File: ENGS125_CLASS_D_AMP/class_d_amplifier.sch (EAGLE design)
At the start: 23 parts, among them J1 BANANA_JACK_CT3151, J2 BANANA_JACK_CT3151, J3 BANANA_JACK_CT3151, J4 BANANA_JACK_CT3151, J5 BANANA_JACK_CT3151, J6 BANANA_JACK_CT3151, U1 LTC6992TSOT-23, U2 LTC4449

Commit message: Initial placement of switching node components
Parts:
- added C8: 0.1u, Engs125_library:C-US
- renumbered U$1 to M1, U$2 to M2
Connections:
- net GND: now also C8.2
- net VOUT: now also C8.1
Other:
- moved on the sheet: J5, J6
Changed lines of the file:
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@@
 <part name="J4" library="Engs125_lib_UPDATEFeb22" deviceset="BANANA_JACK_CT3151" device=""/>
 <part name="SUPPLY8" library="Engs125_library" deviceset="GND" device=""/>
-<part name="J5" library="Engs125_lib_UPDATEFeb22" deviceset="BANANA_JACK_CT3151" device=""/>
-<part name="J6" library="Engs125_lib_UPDATEFeb22" deviceset="BANANA_JACK_CT3151" device=""/>
 <part name="U1" library="Engs125_lib_UPDATEFeb22" deviceset="LTC6992" device="TSOT-23"/>
 <part name="R1" library="Engs125_lib_UPDATEFeb22" deviceset="TRIM_US-" device="CT6"/>
 <part name="R2" library="Engs125_lib_UPDATEFeb22" deviceset="R-US" device="" value=""/>
 <part name="JP2" library="Engs125_lib_UPDATEFeb22" deviceset="PINHD-1X1" device=""/>
-<part name="U$1" library="Engs125_lib_UPDATEFeb22" deviceset="BSC050NE2LSATMA1" device=""/>
-<part name="U$2" library="Engs125_lib_UPDATEFeb22" deviceset="BSC050NE2LSATMA1" device=""/>
+<part name="M1" library="Engs125_lib_UPDATEFeb22" deviceset="BSC050NE2LSATMA1" device=""/>
+<part name="M2" library="Engs125_lib_UPDATEFeb22" deviceset="BSC050NE2LSATMA1" device=""/>
+<part name="J5" library="Engs125_lib_UPDATEFeb22" deviceset="BANANA_JACK_CT3151" device=""/>
+<part name="J6" library="Engs125_lib_UPDATEFeb22" deviceset="BANANA_JACK_CT3151" device=""/>
+<part name="C8" library="Engs125_library" deviceset="C-US" device="" value="0.1u"/>
 </parts>
 <sheets>
@@
 <plain>
 <text x="124.46" y="157.48" size="1.778" layer="97">Input Supply: 12V</text>
-<text x="215.9" y="71.12" size="1.778" layer="97">Output Voltage: 6Vdc
+<text x="15.24" y="132.08" size="1.778" layer="97">Gate Supply: 5V</text>
+<text x="58.674" y="23.622" size="1.778" layer="97">Audio Input: 0V to 1V</text>
+<text x="58.42" y="43.18" size="1.778" layer="97">PWM Output Probe</text>
+<text x="231.14" y="71.12" size="1.778" layer="97">Output Voltage: 6Vdc
 Voltage Ripple: 100mVpp
 &gt; 95% Efficiency
 @1.5A DC load current (4Ω load)</text>
-<text x="15.24" y="132.08" size="1.778" layer="97">Gate Supply: 5V</text>
-<text x="58.674" y="23.622" size="1.778" layer="97">Audio Input: 0V to 1V</text>
-<text x="58.42" y="43.18" size="1.778" layer="97">PWM Output Probe</text>
 </plain>
 <instances>
@@
 <attribute name="VALUE" x="135.255" y="128.905" size="1.778" layer="96"/>
 </instance>
-<instance part="J5" gate="G$1" x="198.12" y="78.74" smashed="yes" rot="R180">
-<attribute name="VALUE" x="198.82" y="82.24" size="0.8128" layer="96" rot="R180"/>
-<attribute name="NAME" x="198.72" y="83.54" size="0.8128" layer="95" rot="R180"/>
-</instance>
-<instance part="J6" gate="G$1" x="198.12" y="71.12" smashed="yes" rot="MR0">
-<attribute name="VALUE" x="198.82" y="67.62" size="0.8128" layer="96" rot="MR0"/>
-<attribute name="NAME" x="198.72" y="66.32" size="0.8128" layer="95" rot="MR0"/>
-</instance>
 <instance part="U1" gate="G$1" x="20.32" y="53.34" smashed="yes">
 <attribute name="NAME" x="10.16" y="66.04" size="1.778" layer="95"/>
@@
 <attribute name="VALUE" x="57.15" y="43.18" size="1.778" layer="96"/>
 </instance>
-<instance part="U$1" gate="G$1" x="124.46" y="93.98" smashed="yes">
+<instance part="M1" gate="G$1" x="124.46" y="93.98" smashed="yes">
 <attribute name="NAME" x="116.84" y="99.06" size="1.778" layer="96"/>
 <attribute name="VALUE" x="137.16" y="93.98" size="1.778" layer="96"/>
 </instance>
-<instance part="U$2" gate="G$1" x="124.46" y="66.04" smashed="yes">
+<instance part="M2" gate="G$1" x="124.46" y="66.04" smashed="yes">
 <attribute name="NAME" x="116.84" y="71.12" size="1.778" layer="96"/>
 <attribute name="VALUE" x="137.16" y="63.5" size="1.778" layer="96"/>
+</instance>
+<instance part="J5" gate="G$1" x="213.36" y="78.74" smashed="yes" rot="R180">
+<attribute name="VALUE" x="214.06" y="82.24" size="0.8128" layer="96" rot="R180"/>
+<attribute name="NAME" x="213.96" y="83.54" size="0.8128" layer="95" rot="R180"/>
+</instance>
+<instance part="J6" gate="G$1" x="213.36" y="71.12" smashed="yes" rot="MR0">
+<attribute name="VALUE" x="214.06" y="67.62" size="0.8128" layer="96" rot="MR0"/>
+<attribute name="NAME" x="213.96" y="66.32" size="0.8128" layer="95" rot="MR0"/>
+</instance>
+<instance part="C8" gate="G$1" x="187.96" y="71.12" smashed="yes">
+<attribute name="NAME" x="188.976" y="71.755" size="1.778" layer="95"/>
+<attribute name="VALUE" x="188.976" y="66.929" size="1.778" layer="96"/>
 </instance>
 </instances>
@@
 <pinref part="C6" gate="G$1" pin="2"/>
 <wire x1="177.8" y1="66.04" x2="177.8" y2="60.96" width="0.1524" layer="91"/>
-<wire x1="177.8" y1="60.96" x2="185.42" y2="60.96" width="0.1524" layer="91"/>
+<wire x1="200.66" y1="60.96" x2="200.66" y2="71.12" width="0.1524" layer="91"/>
+<pinref part="J6" gate="G$1" pin="IN"/>
+<wire x1="200.66" y1="71.12" x2="205.74" y2="71.12" width="0.1524" layer="91"/>
+<wire x1="200.66" y1="60.96" x2="187.96" y2="60.96" width="0.1524" layer="91"/>
 <junction x="177.8" y="60.96"/>
-<wire x1="185.42" y1="60.96" x2="185.42" y2="71.12" width="0.1524" layer="91"/>
-<pinref part="J6" gate="G$1" pin="IN"/>
-<wire x1="185.42" y1="71.12" x2="190.5" y2="71.12" width="0.1524" layer="91"/>
+<pinref part="C8" gate="G$1" pin="2"/>
+<wire x1="187.96" y1="60.96" x2="177.8" y2="60.96" width="0.1524" layer="91"/>
+<wire x1="187.96" y1="66.04" x2="187.96" y2="60.96" width="0.1524" layer="91"/>
+<junction x="187.96" y="60.96"/>
 </segment>
 <segment>
@@
 <wire x1="96.52" y1="60.96" x2="114.3" y2="60.96" width="0.1524" layer="91"/>
 <wire x1="114.3" y1="60.96" x2="114.3" y2="50.8" width="0.1524" layer="91"/>
-<pinref part="U$2" gate="G$1" pin="S"/>
-<pinref part="U$2" gate="G$1" pin="S2"/>
+<pinref part="M2" gate="G$1" pin="S"/>
+<pinref part="M2" gate="G$1" pin="S2"/>
 <wire x1="134.62" y1="53.34" x2="132.08" y2="53.34" width="0.1524" layer="91"/>
 <junction x="129.54" y="53.34"/>
-<pinref part="U$2" gate="G$1" pin="S1"/>
+<pinref part="M2" gate="G$1" pin="S1"/>
 <wire x1="132.08" y1="53.34" x2="129.54" y2="53.34" width="0.1524" layer="91"/>
 <junction x="132.08" y="53.34"/>
@@
 <junction x="101.6" y="78.74"/>
 <label x="134.62" y="78.74" size="1.778" layer="95"/>
-<pinref part="U$1" gate="G$1" pin="S"/>
-<pinref part="U$2" gate="G$1" pin="D"/>
-<pinref part="U$2" gate="G$1" pin="D2"/>
+<pinref part="M1" gate="G$1" pin="S"/>
+<pinref part="M2" gate="G$1" pin="D"/>
+<pinref part="M2" gate="G$1" pin="D2"/>
 <wire x1="134.62" y1="76.2" x2="132.08" y2="76.2" width="0.1524" layer="91"/>
 <junction x="129.54" y="76.2"/>
-<pinref part="U$2" gate="G$1" pin="D1"/>
+<pinref part="M2" gate="G$1" pin="D1"/>
 <wire x1="132.08" y1="76.2" x2="129.54" y2="76.2" width="0.1524" layer="91"/>
 <junction x="132.08" y="76.2"/>
-<pinref part="U$1" gate="G$1" pin="S2"/>
+<pinref part="M1" gate="G$1" pin="S2"/>
 <wire x1="134.62" y1="81.28" x2="132.08" y2="81.28" width="0.1524" layer="91"/>
 <junction x="129.54" y="81.28"/>
-<pinref part="U$1" gate="G$1" pin="S1"/>
+<pinref part="M1" gate="G$1" pin="S1"/>
 <wire x1="132.08" y1="81.28" x2="129.54" y2="81.28" width="0.1524" layer="91"/>
 <junction x="132.08" y="81.28"/>
-</segment>
-</net>
-<net name="VOUT" class="0">
-<segment>
-<pinref part="L1" gate="G$1" pin="2"/>
-<wire x1="162.56" y1="78.74" x2="167.64" y2="78.74" width="0.1524" layer="91"/>
-<label x="170.18" y="78.74" size="1.778" layer="95"/>
-<pinref part="C2" gate="G$1" pin="1"/>
-<wire x1="167.64" y1="78.74" x2="177.8" y2="78.74" width="0.1524" layer="91"/>
-<wire x1="167.64" y1="78.74" x2="167.64" y2="73.66" width="0.1524" layer="91"/>
-<junction x="167.64" y="78.74"/>
-<pinref part="C6" gate="G$1" pin="1"/>
-<wire x1="177.8" y1="78.74" x2="177.8" y2="73.66" width="0.1524" layer="91"/>
-<junction x="177.8" y="78.74"/>
-<pinref part="J5" gate="G$1" pin="IN"/>
-<wire x1="190.5" y1="78.74" x2="177.8" y2="78.74" width="0.1524" layer="91"/>
 </segment>
 </net>
@@
 <wire x1="109.22" y1="129.54" x2="109.22" y2="124.46" width="0.1524" layer="91"/>
 <pinref part="J3" gate="G$1" pin="IN"/>
-<pinref part="U$1" gate="G$1" pin="D"/>
-<pinref part="U$1" gate="G$1" pin="D2"/>
+<pinref part="M1" gate="G$1" pin="D"/>
+<pinref part="M1" gate="G$1" pin="D2"/>
 <wire x1="134.62" y1="104.14" x2="132.08" y2="104.14" width="0.1524" layer="91"/>
 <junction x="129.54" y="104.14"/>
-<pinref part="U$1" gate="G$1" pin="D1"/>
+<pinref part="M1" gate="G$1" pin="D1"/>
 <wire x1="132.08" y1="104.14" x2="129.54" y2="104.14" width="0.1524" layer="91"/>
 <junction x="132.08" y="104.14"/>
@@
 <wire x1="96.52" y1="66.04" x2="111.76" y2="66.04" width="0.1524" layer="91"/>
 <label x="104.14" y="66.04" size="1.778" layer="95"/>
-<pinref part="U$2" gate="G$1" pin="G"/>
+<pinref part="M2" gate="G$1" pin="G"/>
 </segment>
 </net>
@@
 <wire x1="96.52" y1="93.98" x2="111.76" y2="93.98" width="0.1524" layer="91"/>
 <label x="104.14" y="93.98" size="1.778" layer="95"/>
-<pinref part="U$1" gate="G$1" pin="G"/>
+<pinref part="M1" gate="G$1" pin="G"/>
 </segment>
 </net>
@@
 </segment>
 </net>
+<net name="VOUT" class="0">
+<segment>
+<pinref part="J5" gate="G$1" pin="IN"/>
+<wire x1="205.74" y1="78.74" x2="187.96" y2="78.74" width="0.1524" layer="91"/>
+<pinref part="L1" gate="G$1" pin="2"/>
+<wire x1="162.56" y1="78.74" x2="167.64" y2="78.74" width="0.1524" layer="91"/>
+<label x="170.18" y="78.74" size="1.778" layer="95"/>
+<pinref part="C2" gate="G$1" pin="1"/>
+<wire x1="167.64" y1="78.74" x2="177.8" y2="78.74" width="0.1524" layer="91"/>
+<wire x1="167.64" y1="78.74" x2="167.64" y2="73.66" width="0.1524" layer="91"/>
+<junction x="167.64" y="78.74"/>
+<pinref part="C6" gate="G$1" pin="1"/>
+<wire x1="177.8" y1="78.74" x2="177.8" y2="73.66" width="0.1524" layer="91"/>
+<pinref part="C8" gate="G$1" pin="1"/>
+<wire x1="187.96" y1="73.66" x2="187.96" y2="78.74" width="0.1524" layer="91"/>
+<wire x1="187.96" y1="78.74" x2="177.8" y2="78.74" width="0.1524" layer="91"/>
+<junction x="177.8" y="78.74"/>
+<junction x="187.96" y="78.74"/>
+</segment>
+</net>

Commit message: Generatedtop layer power polygons and placed vias
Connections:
- net VIN: now also M1.D3, M1.D4
- net VSW: now also M2.D3, M2.D4
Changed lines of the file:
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@@
 <wire x1="132.08" y1="81.28" x2="129.54" y2="81.28" width="0.1524" layer="91"/>
 <junction x="132.08" y="81.28"/>
+<pinref part="M2" gate="G$1" pin="D4"/>
+<wire x1="134.62" y1="76.2" x2="137.16" y2="76.2" width="0.1524" layer="91"/>
+<junction x="134.62" y="76.2"/>
+<pinref part="M2" gate="G$1" pin="D3"/>
+<wire x1="137.16" y1="76.2" x2="139.7" y2="76.2" width="0.1524" layer="91"/>
+<junction x="137.16" y="76.2"/>
 </segment>
 </net>
@@
 <wire x1="132.08" y1="104.14" x2="129.54" y2="104.14" width="0.1524" layer="91"/>
 <junction x="132.08" y="104.14"/>
+<pinref part="M1" gate="G$1" pin="D4"/>
+<wire x1="134.62" y1="104.14" x2="137.16" y2="104.14" width="0.1524" layer="91"/>
+<junction x="134.62" y="104.14"/>
+<pinref part="M1" gate="G$1" pin="D3"/>
+<wire x1="137.16" y1="104.14" x2="139.7" y2="104.14" width="0.1524" layer="91"/>
+<junction x="137.16" y="104.14"/>
 </segment>
 </net>

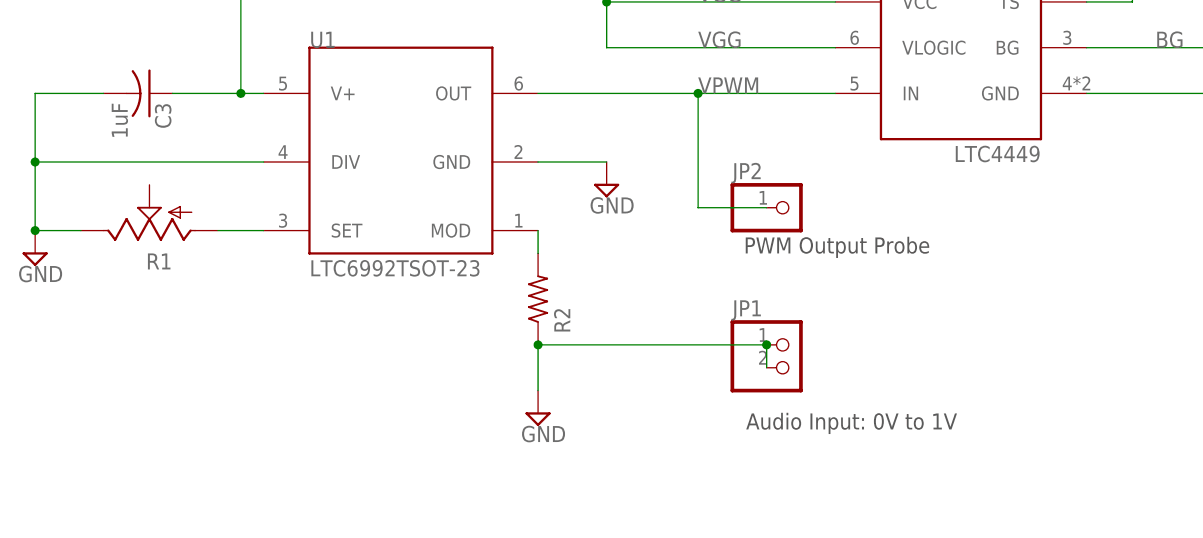
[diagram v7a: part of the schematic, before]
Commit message: Refined placement of gate driver and PWM modulator ICs
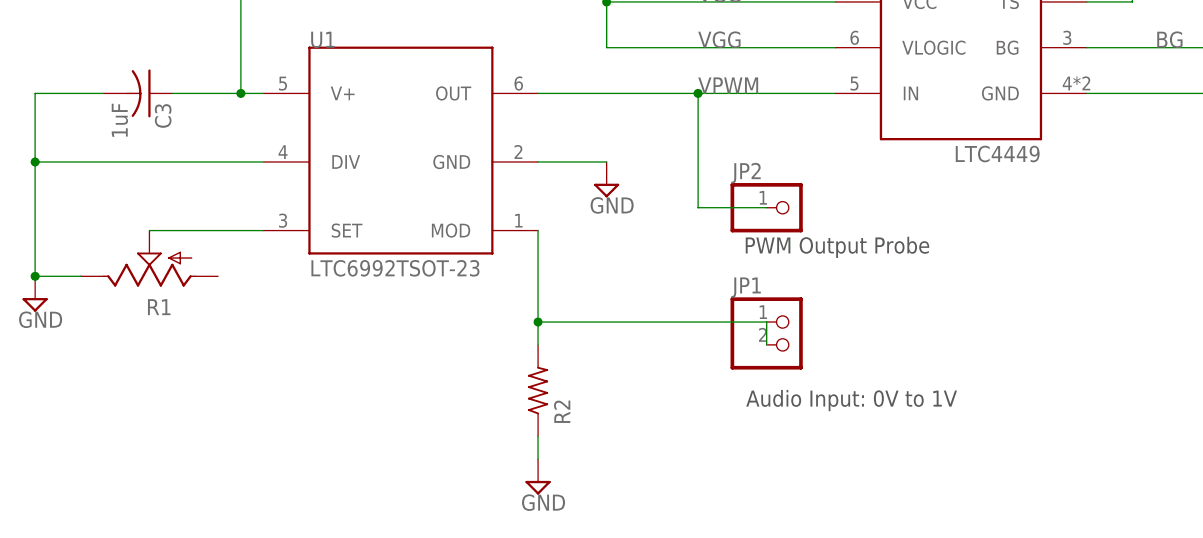
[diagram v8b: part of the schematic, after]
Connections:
- net GND: no longer JP1.1, JP1.2
- net N$1: now also R1.S; no longer R1.A
- net N$4: now also JP1.1, JP1.2
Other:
- moved on the sheet: JP1, R1, R2
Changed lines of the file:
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@@
 <text x="124.46" y="157.48" size="1.778" layer="97">Input Supply: 12V</text>
 <text x="15.24" y="132.08" size="1.778" layer="97">Gate Supply: 5V</text>
-<text x="58.674" y="23.622" size="1.778" layer="97">Audio Input: 0V to 1V</text>
+<text x="58.674" y="26.162" size="1.778" layer="97">Audio Input: 0V to 1V</text>
 <text x="58.42" y="43.18" size="1.778" layer="97">PWM Output Probe</text>
 <text x="231.14" y="71.12" size="1.778" layer="97">Output Voltage: 6Vdc
@@
 <attribute name="VALUE" x="91.44" y="53.34" size="1.778" layer="96" rot="MR0"/>
 </instance>
-<instance part="SUPPLY1" gate="GND" x="-20.32" y="43.18" smashed="yes">
-<attribute name="VALUE" x="-22.225" y="40.005" size="1.778" layer="96"/>
+<instance part="SUPPLY1" gate="GND" x="-20.32" y="38.1" smashed="yes">
+<attribute name="VALUE" x="-22.225" y="34.925" size="1.778" layer="96"/>
 </instance>
 <instance part="C3" gate="G$1" x="-7.62" y="60.96" smashed="yes" rot="R270">
@@
 <attribute name="VALUE" x="41.275" y="47.625" size="1.778" layer="96"/>
 </instance>
-<instance part="SUPPLY3" gate="GND" x="35.56" y="25.4" smashed="yes">
-<attribute name="VALUE" x="33.655" y="22.225" size="1.778" layer="96"/>
+<instance part="SUPPLY3" gate="GND" x="35.56" y="17.78" smashed="yes">
+<attribute name="VALUE" x="33.655" y="14.605" size="1.778" layer="96"/>
 </instance>
 <instance part="SUPPLY4" gate="GND" x="25.4" y="106.68" smashed="yes">
@@
 <attribute name="VALUE" x="168.656" y="66.929" size="1.778" layer="96"/>
 </instance>
-<instance part="JP1" gate="G$1" x="63.5" y="30.48" smashed="yes">
-<attribute name="NAME" x="57.15" y="36.195" size="1.778" layer="95"/>
-<attribute name="VALUE" x="57.15" y="25.4" size="1.778" layer="96"/>
+<instance part="JP1" gate="G$1" x="63.5" y="33.02" smashed="yes">
+<attribute name="NAME" x="57.15" y="38.735" size="1.778" layer="95"/>
+<attribute name="VALUE" x="57.15" y="27.94" size="1.778" layer="96"/>
 </instance>
 <instance part="J1" gate="G$1" x="17.78" y="119.38" smashed="yes" rot="R270">
@@
 <attribute name="VALUE" x="10.16" y="40.64" size="1.778" layer="96"/>
 </instance>
-<instance part="R1" gate="G$1" x="-7.62" y="45.72" smashed="yes" rot="R90">
-<attribute name="NAME" x="-5.08" y="43.18" size="1.778" layer="95" rot="R180"/>
-<attribute name="VALUE" x="-5.08" y="43.18" size="1.778" layer="96" rot="R180"/>
-</instance>
-<instance part="R2" gate="G$1" x="35.56" y="38.1" smashed="yes" rot="R90">
-<attribute name="NAME" x="39.1414" y="34.29" size="1.778" layer="95" rot="R90"/>
-<attribute name="VALUE" x="38.862" y="34.29" size="1.778" layer="96" rot="R90"/>
+<instance part="R1" gate="G$1" x="-7.62" y="40.64" smashed="yes" rot="R90">
+<attribute name="NAME" x="-5.08" y="38.1" size="1.778" layer="95" rot="R180"/>
+<attribute name="VALUE" x="-5.08" y="38.1" size="1.778" layer="96" rot="R180"/>
+</instance>
+<instance part="R2" gate="G$1" x="35.56" y="27.94" smashed="yes" rot="R90">
+<attribute name="NAME" x="39.1414" y="24.13" size="1.778" layer="95" rot="R90"/>
+<attribute name="VALUE" x="38.862" y="24.13" size="1.778" layer="96" rot="R90"/>
 </instance>
 <instance part="JP2" gate="G$1" x="63.5" y="48.26" smashed="yes">
@@
 </busses>
 <nets>
-<net name="N$1" class="0">
-<segment>
-<wire x1="5.08" y1="45.72" x2="0" y2="45.72" width="0.1524" layer="91"/>
-<pinref part="U1" gate="G$1" pin="SET"/>
-<pinref part="R1" gate="G$1" pin="A"/>
-</segment>
-</net>
 <net name="GND" class="0">
 <segment>
 <pinref part="SUPPLY1" gate="GND" pin="GND"/>
-<wire x1="-15.24" y1="45.72" x2="-20.32" y2="45.72" width="0.1524" layer="91"/>
+<wire x1="-15.24" y1="40.64" x2="-20.32" y2="40.64" width="0.1524" layer="91"/>
 <wire x1="5.08" y1="53.34" x2="-20.32" y2="53.34" width="0.1524" layer="91"/>
-<wire x1="-20.32" y1="53.34" x2="-20.32" y2="45.72" width="0.1524" layer="91"/>
-<junction x="-20.32" y="45.72"/>
+<wire x1="-20.32" y1="53.34" x2="-20.32" y2="40.64" width="0.1524" layer="91"/>
+<junction x="-20.32" y="40.64"/>
 <pinref part="C3" gate="G$1" pin="2"/>
 <wire x1="-12.7" y1="60.96" x2="-20.32" y2="60.96" width="0.1524" layer="91"/>
@@
 </segment>
 <segment>
-<pinref part="JP1" gate="G$1" pin="2"/>
-<pinref part="JP1" gate="G$1" pin="1"/>
-<wire x1="60.96" y1="33.02" x2="60.96" y2="30.48" width="0.1524" layer="91"/>
 <pinref part="R2" gate="G$1" pin="1"/>
-<wire x1="35.56" y1="33.02" x2="60.96" y2="33.02" width="0.1524" layer="91"/>
-<junction x="60.96" y="33.02"/>
 <pinref part="SUPPLY3" gate="GND" pin="GND"/>
-<wire x1="35.56" y1="33.02" x2="35.56" y2="27.94" width="0.1524" layer="91"/>
-<junction x="35.56" y="33.02"/>
+<wire x1="35.56" y1="22.86" x2="35.56" y2="20.32" width="0.1524" layer="91"/>
 </segment>
 </net>
@@
 </segment>
 </net>
-<net name="N$4" class="0">
-<segment>
-<pinref part="U1" gate="G$1" pin="MOD"/>
-<pinref part="R2" gate="G$1" pin="2"/>
-<wire x1="35.56" y1="45.72" x2="35.56" y2="43.18" width="0.1524" layer="91"/>
-</segment>
-</net>
 <net name="VOUT" class="0">
 <segment>
@@
 </segment>
 </net>
+<net name="N$4" class="0">
+<segment>
+<pinref part="JP1" gate="G$1" pin="2"/>
+<pinref part="JP1" gate="G$1" pin="1"/>
+<wire x1="60.96" y1="35.56" x2="60.96" y2="33.02" width="0.1524" layer="91"/>
+<pinref part="R2" gate="G$1" pin="2"/>
+<pinref part="U1" gate="G$1" pin="MOD"/>
+<wire x1="35.56" y1="45.72" x2="35.56" y2="35.56" width="0.1524" layer="91"/>
+<wire x1="35.56" y1="35.56" x2="35.56" y2="33.02" width="0.1524" layer="91"/>
+<wire x1="60.96" y1="35.56" x2="35.56" y2="35.56" width="0.1524" layer="91"/>
+<junction x="35.56" y="35.56"/>
+</segment>
+</net>
+<net name="N$1" class="0">
+<segment>
+<pinref part="R1" gate="G$1" pin="S"/>
+<pinref part="U1" gate="G$1" pin="SET"/>
+<wire x1="-7.62" y1="45.72" x2="5.08" y2="45.72" width="0.1524" layer="91"/>
+</segment>
+</net>
